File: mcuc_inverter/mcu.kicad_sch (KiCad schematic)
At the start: 0 parts

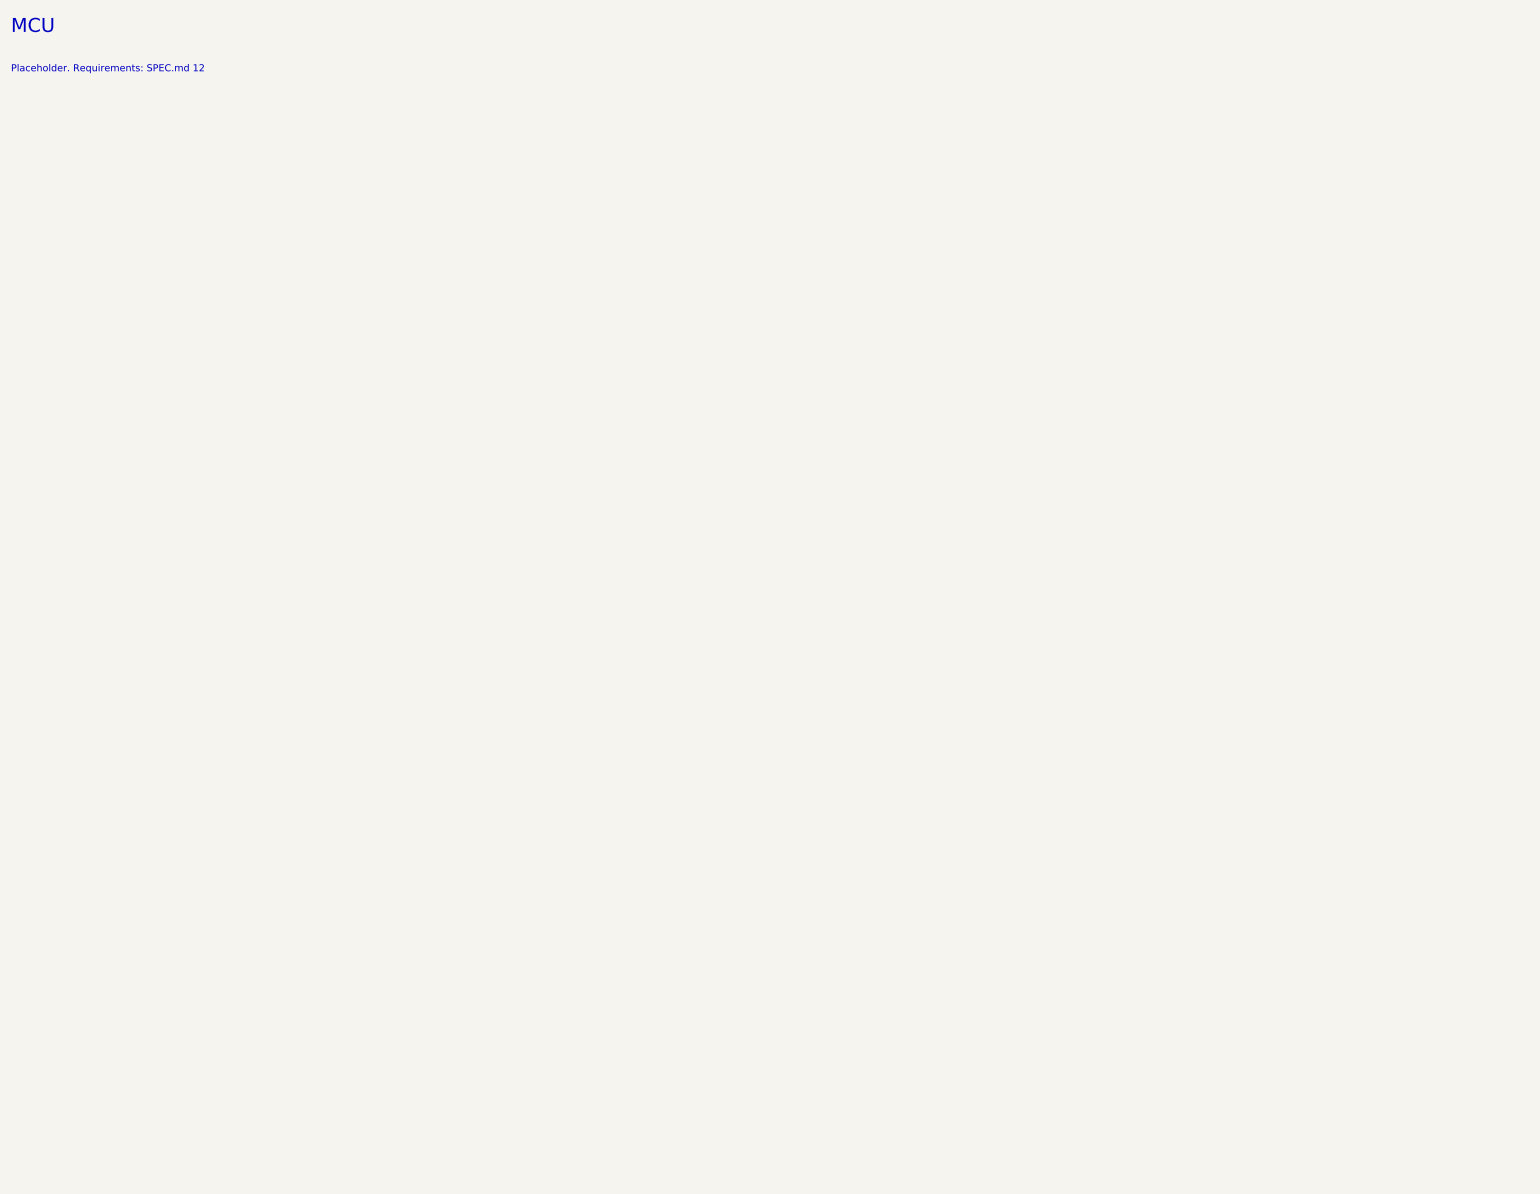
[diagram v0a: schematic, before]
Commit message: Capture MCU sheet: STM32F405VGT6 core circuit, ERC clean
Populate mcuc_inverter/mcu.kicad_sch with the STM32F405VGTx from the
official KiCad 9 library: per-pin VDD decoupling (6x100n + 4.7u bulk),
VDDA/VREF+ via ferrite with 1u+100n, 2x2.2u VCAP, BOOT0 10k pulldown,
NRST 100n, 8 MHz HSE with 18 pF loads, and the SPEC 12.2 anchor pins
as hierarchical labels (TIM1 PWM HS/LS, FAULT_BKIN on PB12, CAN1,
USB, SWD) verified against the symbol pin table via netlist export.

Root sheet gains the 14 matching sheet pins on the MCU sheet symbol.
Project ERC severities: pin_not_connected and label_dangling relaxed
error->warning so future-GPIO pins stay visible without no-connect
flags (CLI ignores exclusions; label_dangling hits a known CLI false
positive on single-pin hierarchical nets, kicad#20528).

ERC: 0 errors, 93 warnings (66 unused GPIOs, 14 empty counterpart
sheets, 13 false-positive dangling labels). PDF export succeeds.

Co-Authored-By: Claude Fable 5 <noreply@anthropic.com>
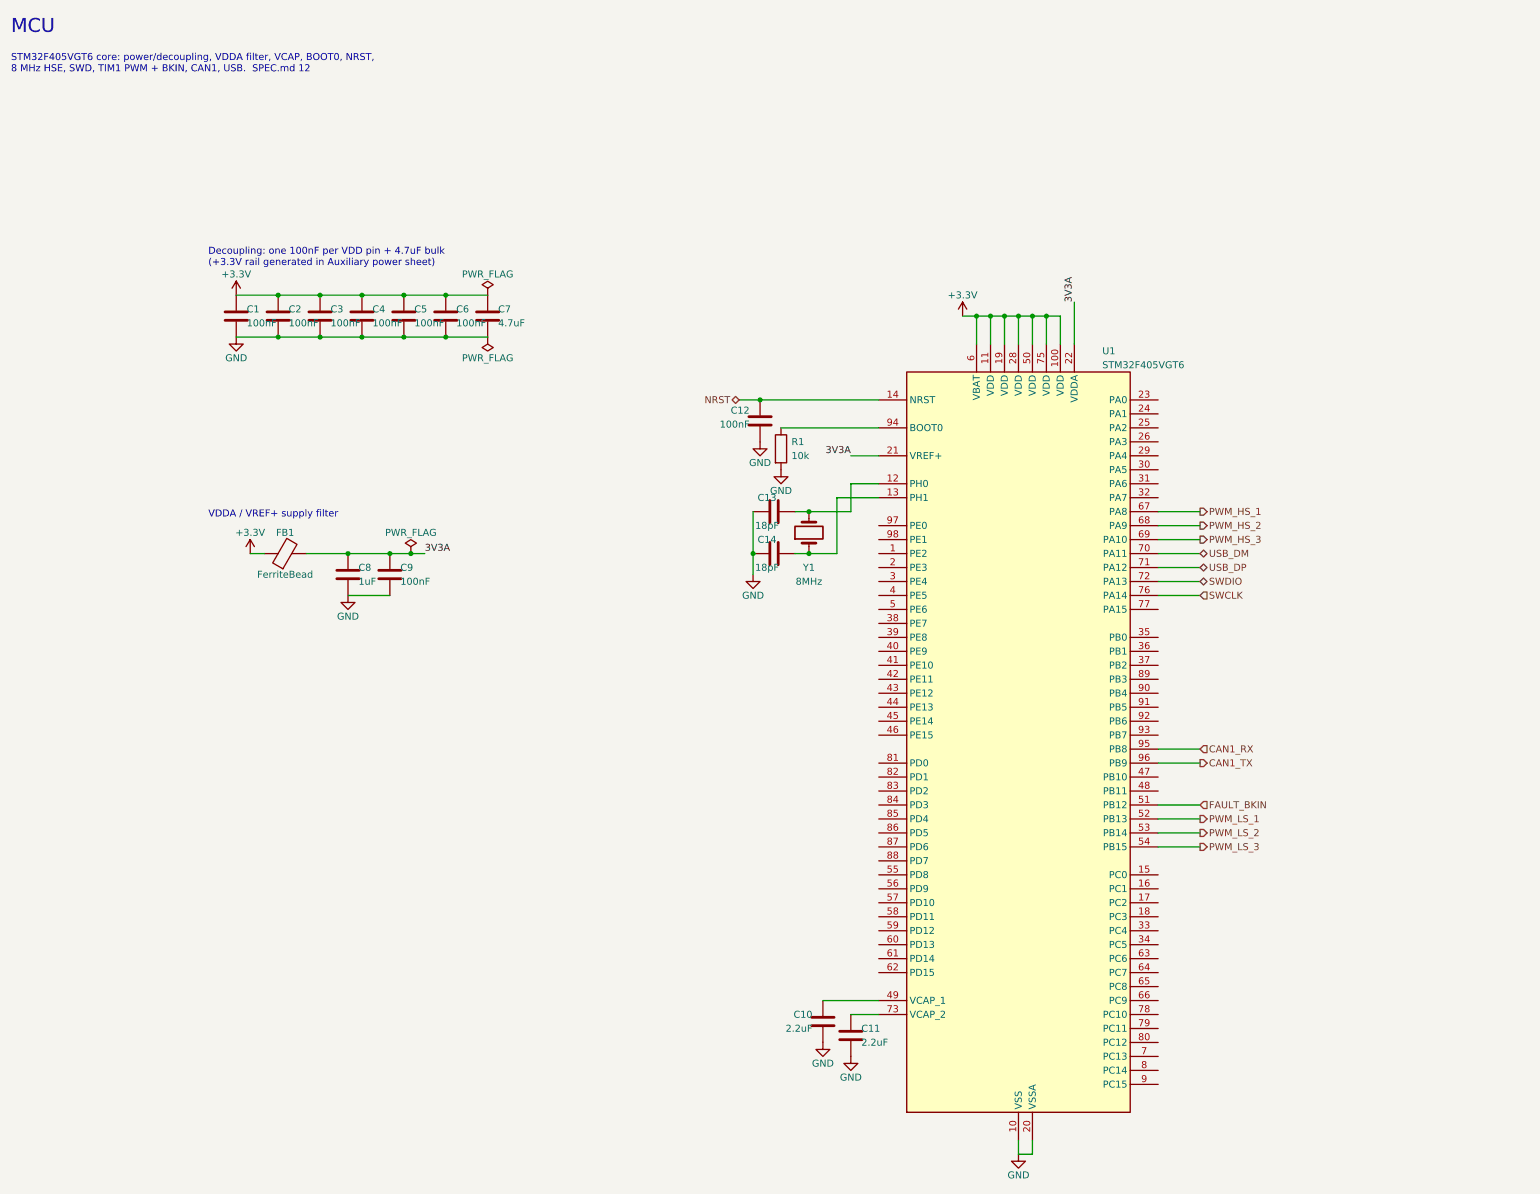
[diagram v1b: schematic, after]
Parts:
- added C1, C12, C2, C3, C4, C5, C6, C9: 100nF, symbol Device:C
- added C10, C11: 2.2uF, symbol Device:C
- added C13, C14: 18pF, symbol Device:C
- added C7: 4.7uF, symbol Device:C
- added C8: 1uF, symbol Device:C
- added FB1: FerriteBead, symbol Device:FerriteBead
- added R1: 10k, symbol Device:R
- added U1: STM32F405VGT6, symbol MCU_ST_STM32F4:STM32F405VGTx
- added Y1: 8MHz, symbol Device:Crystal
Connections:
- new net: C13.2, U1.12 (PH0), Y1.2
- new net: C14.2, U1.13 (PH1), Y1.1
- new net: C10.1, U1.49 (VCAP_1)
- new net: C11.1, U1.73 (VCAP_2)
- new net: R1.1, U1.94 (BOOT0)
- new net +3.3V: C1.1, C2.1, C3.1, C4.1, C5.1, C6.1, C7.1, FB1.1, U1.100 (VDD), U1.11 (VDD), U1.19 (VDD), U1.28 (VDD), U1.50 (VDD), U1.6 (VBAT), U1.75 (VDD)
- new net 3V3A: C8.1, C9.1, FB1.2, U1.21 (VREF+), U1.22 (VDDA)
- new net CAN1_RX: U1.95 (PB8)
- new net CAN1_TX: U1.96 (PB9)
- new net FAULT_BKIN: U1.51 (PB12)
- new net GND: C1.2, C10.2, C11.2, C12.2, C13.1, C14.1, C2.2, C3.2, C4.2, C5.2, C6.2, C7.2, C8.2, C9.2, R1.2, U1.10 (VSS), U1.20 (VSSA), U1.27 (VSS), U1.74 (VSS), U1.99 (VSS)
- new net NRST: C12.1, U1.14 (NRST)
- new net PWM_HS_1: U1.67 (PA8)
- new net PWM_HS_2: U1.68 (PA9)
- new net PWM_HS_3: U1.69 (PA10)
- new net PWM_LS_1: U1.52 (PB13)
- new net PWM_LS_2: U1.53 (PB14)
- new net PWM_LS_3: U1.54 (PB15)
- new net SWCLK: U1.76 (PA14)
- new net SWDIO: U1.72 (PA13)
- new net USB_DM: U1.70 (PA11)
- new net USB_DP: U1.71 (PA12)
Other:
- note added: "Decoupling: one 100nF per VDD pin + 4.7uF bulk (+3.3V rail generated in Auxiliary power sheet)"
- note added: "STM32F405VGT6 core: power/decoupling, VDDA filter, VCAP, BOOT0, NRST, 8 MHz HSE, SWD, TIM1 PWM + BKIN, CAN1, USB. SPEC.md 12"
- note added: "VDDA / VREF+ supply filter"
- note removed: "Placeholder. Requirements: SPEC.md 12"

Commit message: Capture aux_power sheet: full D020 rail tree, 7 blocks
INN3990CQ flyback per datasheet Fig. 10 / DER-948Q (series-string
input films, RCD clamp, custom 3-winding transformer symbol with
Lp/VOR/isolation notes, bias->BPP, Schottky secondary, FB 143k/13.2k
-> 14.97 V, SR and IS tied to GND per datasheet for diode operation);
LM5175 buck-boost aux path (15.02 V, deliberately above the
diode-dropped flyback so aux carries the load when present) through
LM74610-Q1 + external FET; two LMR51430 bucks (5 V: 71.5k/9.76k;
12 V: 115k/6.04k); TLV1117-33 3.3 V (PWR_FLAG moved here from the
MCU sheet - this is the rail's true source); 4x SN6505B + WE
750316856 gate supplies (winding CT pinout verified from the WE
drawing; +17.9/-5.1 zener splits); NXE2S0505MC isolated CAN 5 V.

All 12 VGD nets verified in the netlist to span aux_power sources
and gate_drive loads (e.g. VGD_HS1_P = rectifiers + caps + U301
VCC2), independently re-checked before commit. ERC 0 errors.

Co-Authored-By: Claude Fable 5 <noreply@anthropic.com>
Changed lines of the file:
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@@
-	(symbol
-		(lib_id "power:PWR_FLAG")
-		(at 106.68 67.31 0)
-		(unit 1)
-		(exclude_from_sim no)
-		(in_bom no)
-		(on_board yes)
-		(dnp no)
-		(fields_autoplaced yes)
-		(property "Reference" "#FLG01"
-			(at 108.585 66.04 0)
-			(effects
-				(font
-					(size 1.27 1.27)
-				)
-				(justify left)
-				(hide yes)
-			)
-		)
-		(property "Value" "PWR_FLAG"
-			(at 106.68 63.5 0)
-			(effects
-				(font
-					(size 1.27 1.27)
-				)
-			)
-		)
-		(property "Footprint" ""
-			(at 106.68 67.31 0)
-			(effects
-				(font
-					(size 1.27 1.27)
-				)
-				(hide yes)
-			)
-		)
-		(property "Datasheet" "~"
-			(at 106.68 67.31 0)
-			(effects
-				(font
-					(size 1.27 1.27)
-				)
-				(hide yes)
-			)
-		)
-		(property "Description" ""
-			(at 106.68 67.31 0)
-			(effects
-				(font
-					(size 1.27 1.27)
-				)
-				(hide yes)
-			)
-		)
-		(pin "1"
-		)
-		(instances
-			(project "mcuc_inverter"
-				(path "/689a95c8-82a6-4e82-9207-262af70daca3/cf4c33cf-43f9-478b-899e-44632328b324"
-					(reference "#FLG01")
-					(unit 1)
-				)
-			)
-		)
-	)
 	(symbol
 		(lib_id "power:PWR_FLAG")

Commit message: Wire full MCU pin map; add verified PINOUT.md
All 33 remaining signals wired per the citation-verified map (D023):
phase currents PC0/1/2 on VESC triple-simultaneous ADC channels,
V_BUS PC3, temps PA3/PB0/PC4, SinCos PA5/PA6, I_REF PA4/PA7/PB1,
encoder PC6/7/8 (TIM3), halls PD12/13/14, resolver SPI3 PC10/PC11 +
PA15 boot-safe CS + PD0/PD1/PD2 controls, supervisor GPIOs PD3/4/5,
precharge/contactor/discharge PE2/3/4, LED PE0, VBUS sense PC5, PPM
PB6 (TIM4_CH1, VESC convention - repurposed J1206 spare pin).
PA0/1/2 and PB10/11 reserved with on-sheet notes.

AD2S1205 drive validated in-datasheet: VIH 2.0 V @ 5 V supply, so
3.3 V MCU outputs are legal; its 5 V outputs land on FT pins only.

docs/PINOUT.md: complete table with per-row DS8626 Table 7/9
citations, 5V-tolerance column with the analog-mode caveat, and the
D023 reservations - generated against the post-wiring netlist.

ERC 0 errors (warnings down 224 -> 201 as dangling pins connected).
33/33 nets machine-verified U1-pad-to-counterpart; 6 re-verified
independently before commit.

Co-Authored-By: Claude Fable 5 <noreply@anthropic.com>
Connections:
- net PRECHARGE_EN: now reaches U1.1 (PE2)
- net I_PH_1: now reaches U1.15 (PC0)
- net I_PH_2: now reaches U1.16 (PC1)
- net I_PH_3: now reaches U1.17 (PC2)
- net V_BUS: now reaches U1.18 (PC3)
- net CONTACTOR_EN: now reaches U1.2 (PE3)
- net TEMP_COLDPLATE: now reaches U1.26 (PA3)
- net I_REF_1: now reaches U1.29 (PA4)
- net DISCHARGE_EN: now reaches U1.3 (PE4)
- net SINCOS_SIN: now reaches U1.30 (PA5)
- net SINCOS_COS: now reaches U1.31 (PA6)
- net I_REF_2: now reaches U1.32 (PA7)
- net MOTOR_TEMP: now reaches U1.33 (PC4)
- net USB_VBUS_SENSE: now reaches U1.34 (PC5)
- net TEMP_BOARD: now reaches U1.35 (PB0)
- net I_REF_3: now reaches U1.36 (PB1)
- net HALL_1: now reaches U1.59 (PD12)
- net HALL_2: now reaches U1.60 (PD13)
- net HALL_3: now reaches U1.61 (PD14)
- net ENC_A: now reaches U1.63 (PC6)
- net ENC_B: now reaches U1.64 (PC7)
- net ENC_I: now reaches U1.65 (PC8)
- net RES_SPI_NCS: now reaches U1.77 (PA15)
- net RES_SPI_SCK: now reaches U1.78 (PC10)
- net RES_SPI_MISO: now reaches U1.79 (PC11)
- net RES_SPI_NSAMPLE: now reaches U1.81 (PD0)
- net RES_SPI_NRDVEL: now reaches U1.82 (PD1)
- net RES_NFAULT: now reaches U1.83 (PD2)
- net OC_LATCHED: now reaches U1.84 (PD3)
- net FAULT_RESET: now reaches U1.85 (PD4)
- net DRV_RST_IN: now reaches U1.86 (PD5)
- net PPM: now reaches U1.92 (PB6)
- net LED_FAULT: now reaches U1.97 (PE0)
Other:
- note added: "PA0 / PA1 / PA2 (pins 23/24/25): reserved SENS1/2/3 phase-voltage inputs, not fitted (DECISIONS.md D023)"
- note added: "PB10 / PB11 (pins 47/48): reserved UART3 / I2C2 expansion (D023)"

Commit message: Board-prep: footprint audit complete, HV terminals, off-board flags
474-component audit: 466 valid resolved footprints, 13 off-board
exclusions per D024 (caps to carrier, chassis resistors, HOYS), 4
flagged TBDs (custom flyback + 3 unchosen inductors), zero silent
gaps. Netlist-fatal fixes: Q403 renumbered to Wolfspeed TO-263-7
convention (G1/KS2/S3-7/tab-D8), CSD18543Q3A remapped to KiCad's
SSSGD VSON-8 pairing - both verified in the netlist afterward.

New HV interface terminals J401-J405 (M4 ring-lug pads: DC input,
precharge-R chassis loop, discharge-R return, bus taps) and HOYS
harness headers J501-J503 (JST 2mm; PA-vs-PH footprint flagged TBV)
with net membership machine-verified incl. the OC_TRIP wire-OR and
I_REF paths to the MCU ADCs.

ERC 0 errors, warnings 201 -> 200 (none introduced).

Co-Authored-By: Claude Fable 5 <noreply@anthropic.com>
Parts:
- C1, C12, C13, C14, C2, C3, C4, C5, C6, C8, C9: footprint (none) -> Capacitor_SMD:C_0603_1608Metric
- C10, C11, C7: footprint (none) -> Capacitor_SMD:C_0805_2012Metric
- FB1: footprint (none) -> Inductor_SMD:L_0805_2012Metric
- R1: footprint (none) -> Resistor_SMD:R_0603_1608Metric
- U1: footprint (none) -> Package_QFP:LQFP-100_14x14mm_P0.5mm
- Y1: footprint (none) -> Crystal:Crystal_SMD_5032-2Pin_5.0x3.2mm
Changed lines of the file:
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@@
 			)
 		)
-		(property "Footprint" ""
+		(property "Footprint" "Package_QFP:LQFP-100_14x14mm_P0.5mm"
 			(at 203.2 149.86 0)
 			(effects
@@
 			)
 		)
-		(property "Footprint" ""
+		(property "Footprint" "Capacitor_SMD:C_0603_1608Metric"
 			(at 60.96 71.12 0)
 			(effects
@@
 			)
 		)
-		(property "Footprint" ""
+		(property "Footprint" "Capacitor_SMD:C_0603_1608Metric"
 			(at 68.58 71.12 0)
 			(effects
@@
 			)
 		)
-		(property "Footprint" ""
+		(property "Footprint" "Capacitor_SMD:C_0603_1608Metric"
 			(at 76.2 71.12 0)
 			(effects
@@
 			)
 		)
-		(property "Footprint" ""
+		(property "Footprint" "Capacitor_SMD:C_0603_1608Metric"
 			(at 83.82 71.12 0)
 			(effects
@@
 			)
 		)
-		(property "Footprint" ""
+		(property "Footprint" "Capacitor_SMD:C_0603_1608Metric"
 			(at 91.44 71.12 0)
 			(effects
@@
 			)
 		)
-		(property "Footprint" ""
+		(property "Footprint" "Capacitor_SMD:C_0603_1608Metric"
 			(at 99.06 71.12 0)
 			(effects
@@
 			)
 		)
-		(property "Footprint" ""
+		(property "Footprint" "Capacitor_SMD:C_0805_2012Metric"
 			(at 106.68 71.12 0)
 			(effects
@@
 			)
 		)
-		(property "Footprint" ""
+		(property "Footprint" "Inductor_SMD:L_0805_2012Metric"
 			(at 69.85 114.3 0)
 			(effects
@@
 			)
 		)
-		(property "Footprint" ""
+		(property "Footprint" "Capacitor_SMD:C_0603_1608Metric"
 			(at 81.28 118.11 0)
 			(effects
@@
 			)
 		)
-		(property "Footprint" ""
+		(property "Footprint" "Capacitor_SMD:C_0603_1608Metric"
 			(at 88.9 118.11 0)
 			(effects
@@
 			)
 		)
-		(property "Footprint" ""
+		(property "Footprint" "Capacitor_SMD:C_0805_2012Metric"
 			(at 167.64 199.39 0)
 			(effects
@@
 			)
 		)
-		(property "Footprint" ""
+		(property "Footprint" "Capacitor_SMD:C_0805_2012Metric"
 			(at 172.72 201.93 0)
 			(effects
@@
 			)
 		)
-		(property "Footprint" ""
+		(property "Footprint" "Capacitor_SMD:C_0603_1608Metric"
 			(at 156.21 90.17 0)
 			(effects
@@
 			)
 		)
-		(property "Footprint" ""
+		(property "Footprint" "Crystal:Crystal_SMD_5032-2Pin_5.0x3.2mm"
 			(at 165.1 110.49 0)
 			(effects
@@
 			)
 		)
-		(property "Footprint" ""
+		(property "Footprint" "Capacitor_SMD:C_0603_1608Metric"
 			(at 158.75 106.68 0)
 			(effects
@@
 			)
 		)
-		(property "Footprint" ""
+		(property "Footprint" "Capacitor_SMD:C_0603_1608Metric"
 			(at 158.75 114.3 0)
 			(effects
@@
 			)
 		)
-		(property "Footprint" ""
+		(property "Footprint" "Resistor_SMD:R_0603_1608Metric"
 			(at 160.02 95.25 0)
 			(effects
